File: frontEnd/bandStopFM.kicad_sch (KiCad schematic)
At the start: 18 parts, among them U301 BGS12P2L6E6327XTSA1, U302 BGS12P2L6E6327XTSA1

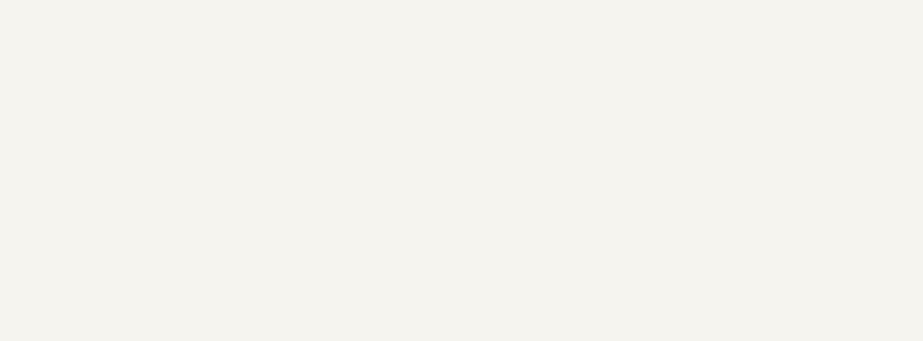
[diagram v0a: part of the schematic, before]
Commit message: update schematics, add bypass for the attenuator
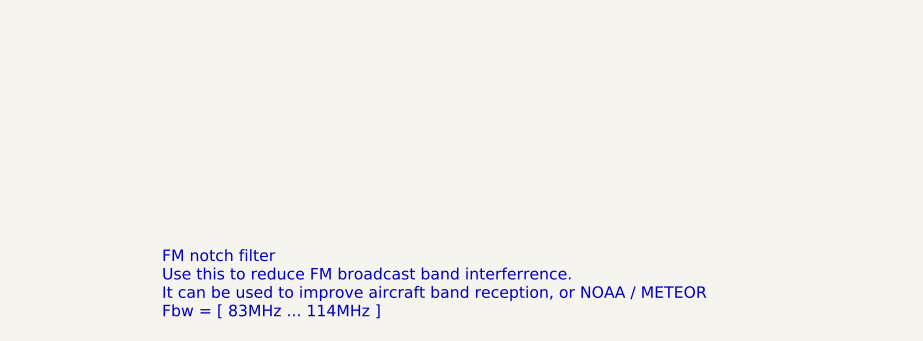
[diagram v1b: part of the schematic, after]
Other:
- note added: "FM notch filter Use this to reduce FM broadcast band interferrence. It can be used to improve aircraft band reception, or NOAA / METEOR Fbw = [ 83MHz ... 114MHz ]"
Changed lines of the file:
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@@
     (stroke (width 0) (type default) (color 0 0 0 0))
+  )
+  (text "FM notch filter\nUse this to reduce FM broadcast band interferrence.\nIt can be used to improve aircraft band reception, or NOAA / METEOR\nFbw = [ 83MHz ... 114MHz ]"
+    (at 180.34 177.8 0)
+    (effects (font (size 1.27 1.27)) (justify left bottom))
   )
   (hierarchical_label "FILTER_ENABLE" (shape input) (at 57.15 83.82 180)

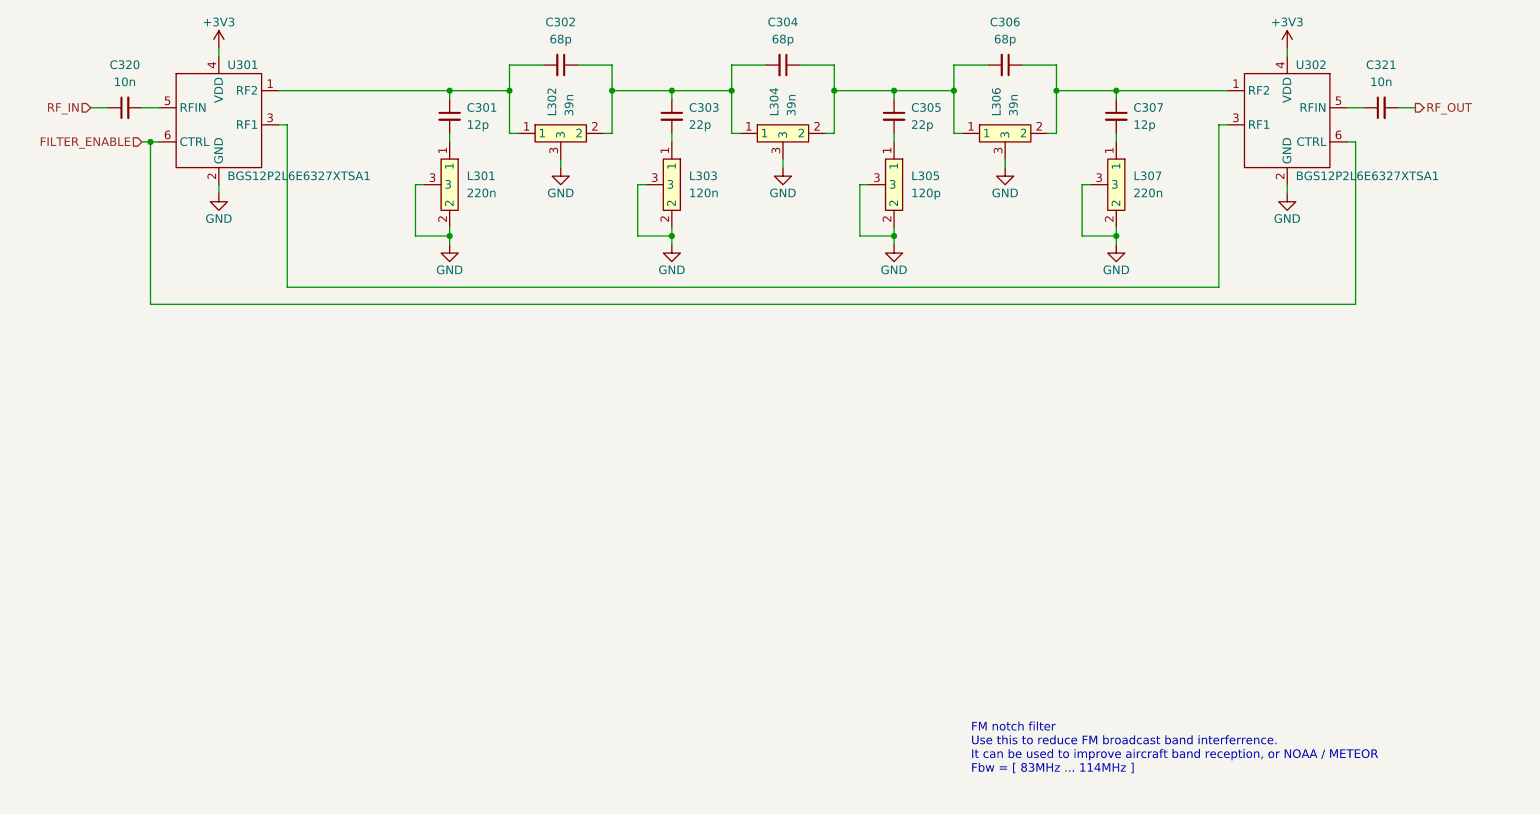
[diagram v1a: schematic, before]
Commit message: simply schematic: remove attenuator and gain blocks; add 5 way multiplexer
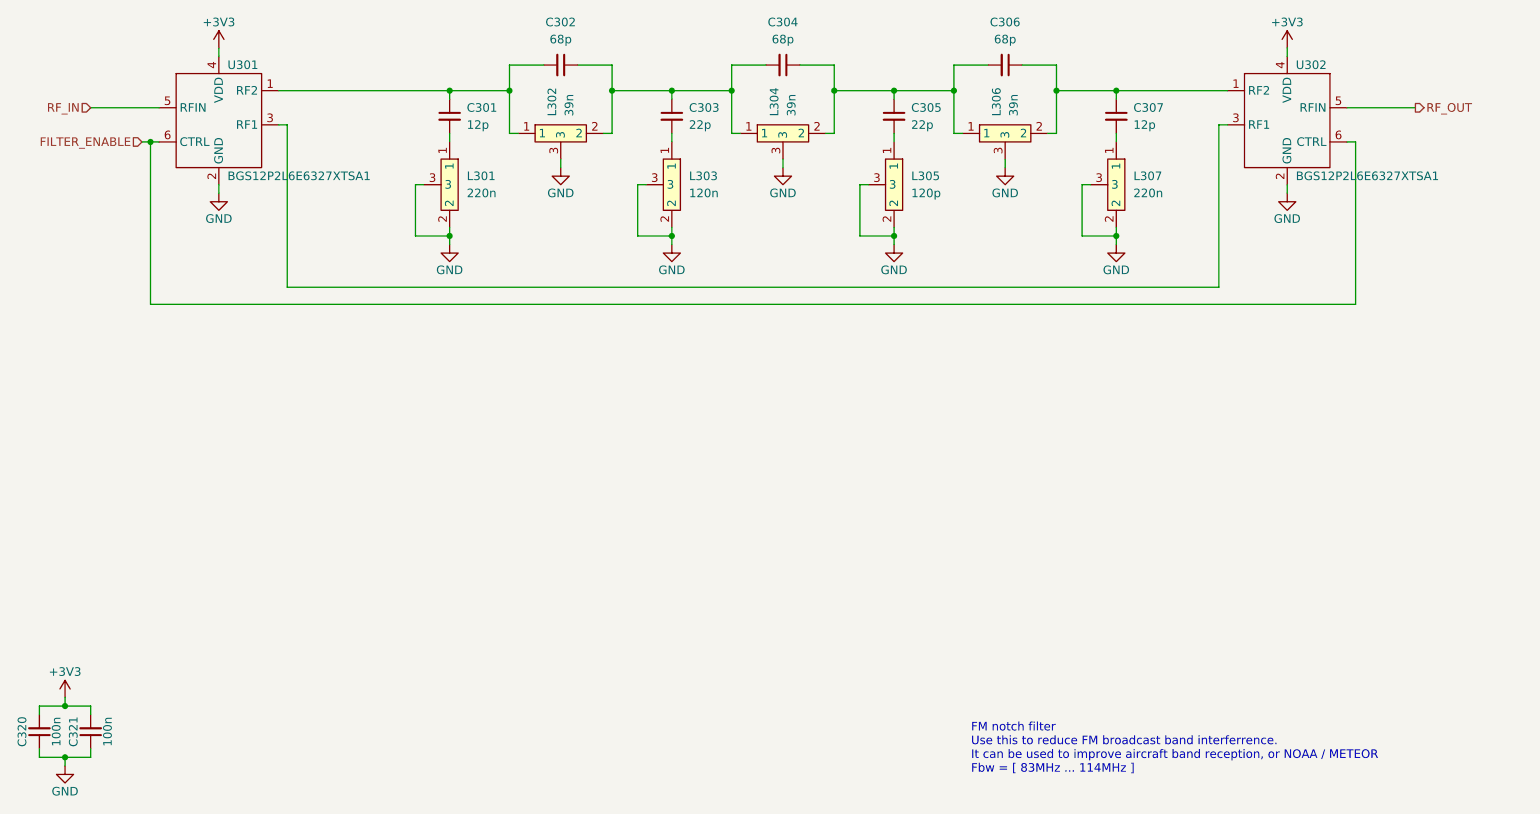
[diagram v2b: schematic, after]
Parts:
- C320, C321: value 10n -> 100n
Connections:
- net +3V3: now also C320.2, C321.2
- net GND: now also C320.1, C321.1
- net RF_IN: now also U301.5 (RFIN); no longer C320.1
- net RF_OUT: now also U302.5 (RFIN); no longer C321.2
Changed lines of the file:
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@@
   (junction (at 193.04 76.2) (diameter 0) (color 0 0 0 0)
   )
+  (junction (at 45.72 167.64) (diameter 0) (color 0 0 0 0)
+  )
   (junction (at 102.87 76.2) (diameter 0) (color 0 0 0 0)
   )
+  (junction (at 45.72 175.26) (diameter 0) (color 0 0 0 0)
+  )
   (junction (at 201.93 97.79) (diameter 0) (color 0 0 0 0)
   )
@@
   (junction (at 201.93 76.2) (diameter 0) (color 0 0 0 0)
   )
+  (wire (pts (xy 41.91 173.99) (xy 41.91 175.26))
+    (stroke (width 0) (type default) (color 0 0 0 0))
+  )
   (wire (pts (xy 152.4 86.36) (xy 152.4 87.63))
     (stroke (width 0) (type default) (color 0 0 0 0))
@@
     (stroke (width 0) (type default) (color 0 0 0 0))
   )
+  (wire (pts (xy 41.91 175.26) (xy 45.72 175.26))
+    (stroke (width 0) (type default) (color 0 0 0 0))
+  )
   (wire (pts (xy 168.91 82.55) (xy 168.91 83.82))
     (stroke (width 0) (type default) (color 0 0 0 0))
@@
     (stroke (width 0) (type default) (color 0 0 0 0))
   )
+  (wire (pts (xy 41.91 168.91) (xy 41.91 167.64))
+    (stroke (width 0) (type default) (color 0 0 0 0))
+  )
   (wire (pts (xy 102.87 97.79) (xy 102.87 99.06))
     (stroke (width 0) (type default) (color 0 0 0 0))
@@
     (stroke (width 0) (type default) (color 0 0 0 0))
   )
-  (wire (pts (xy 57.15 78.74) (xy 59.69 78.74))
+  (wire (pts (xy 45.72 175.26) (xy 45.72 176.53))
     (stroke (width 0) (type default) (color 0 0 0 0))
   )
@@
     (stroke (width 0) (type default) (color 0 0 0 0))
   )
-  (wire (pts (xy 243.84 78.74) (xy 246.38 78.74))
-    (stroke (width 0) (type default) (color 0 0 0 0))
-  )
   (wire (pts (xy 201.93 97.79) (xy 201.93 99.06))
     (stroke (width 0) (type default) (color 0 0 0 0))
@@
     (stroke (width 0) (type default) (color 0 0 0 0))
   )
+  (wire (pts (xy 41.91 167.64) (xy 45.72 167.64))
+    (stroke (width 0) (type default) (color 0 0 0 0))
+  )
   (wire (pts (xy 57.15 83.82) (xy 58.42 83.82))
     (stroke (width 0) (type default) (color 0 0 0 0))
   )
+  (wire (pts (xy 45.72 167.64) (xy 49.53 167.64))
+    (stroke (width 0) (type default) (color 0 0 0 0))
+  )
   (wire (pts (xy 163.83 97.79) (xy 168.91 97.79))
     (stroke (width 0) (type default) (color 0 0 0 0))
@@
     (stroke (width 0) (type default) (color 0 0 0 0))
   )
+  (wire (pts (xy 49.53 167.64) (xy 49.53 168.91))
+    (stroke (width 0) (type default) (color 0 0 0 0))
+  )
   (wire (pts (xy 168.91 76.2) (xy 177.8 76.2))
     (stroke (width 0) (type default) (color 0 0 0 0))
@@
     (stroke (width 0) (type default) (color 0 0 0 0))
   )
+  (wire (pts (xy 49.53 173.99) (xy 49.53 175.26))
+    (stroke (width 0) (type default) (color 0 0 0 0))
+  )
   (wire (pts (xy 165.1 90.17) (xy 163.83 90.17))
     (stroke (width 0) (type default) (color 0 0 0 0))
@@
     (stroke (width 0) (type default) (color 0 0 0 0))
   )
+  (wire (pts (xy 45.72 175.26) (xy 49.53 175.26))
+    (stroke (width 0) (type default) (color 0 0 0 0))
+  )
   (wire (pts (xy 78.74 81.28) (xy 78.74 105.41))
     (stroke (width 0) (type default) (color 0 0 0 0))
@@
     (stroke (width 0) (type default) (color 0 0 0 0))
   )
-  (wire (pts (xy 236.22 78.74) (xy 238.76 78.74))
+  (wire (pts (xy 236.22 78.74) (xy 246.38 78.74))
     (stroke (width 0) (type default) (color 0 0 0 0))
   )
@@
     (stroke (width 0) (type default) (color 0 0 0 0))
   )
-  (wire (pts (xy 49.53 78.74) (xy 52.07 78.74))
+  (wire (pts (xy 49.53 78.74) (xy 59.69 78.74))
+    (stroke (width 0) (type default) (color 0 0 0 0))
+  )
+  (wire (pts (xy 45.72 166.37) (xy 45.72 167.64))
     (stroke (width 0) (type default) (color 0 0 0 0))
   )
@@
     (pin "2")
   )
+  (symbol (lib_id "Device:C_Small") (at 41.91 171.45 180) (unit 1)
+    (in_bom yes) (on_board yes)
+    (property "Reference" "C320" (id 0) (at 39.37 171.45 90))
+    (property "Value" "100n" (id 1) (at 44.45 171.45 90))
+    (property "Footprint" "Capacitor_SMD:C_0805_2012Metric" (id 2) (at 41.91 171.45 0)
+      (effects (font (size 1.27 1.27)) hide)
+    )
+    (property "Datasheet" "~" (id 3) (at 41.91 171.45 0)
+      (effects (font (size 1.27 1.27)) hide)
+    )
+    (pin "1")
+    (pin "2")
+  )
   (symbol (lib_id "frontEnd:DIY_COIL") (at 102.87 90.17 270) (unit 1)
     (in_bom yes) (on_board yes)
@@
     (pin "3")
   )
-  (symbol (lib_id "Device:C_Small") (at 54.61 78.74 90) (unit 1)
-    (in_bom yes) (on_board yes) (fields_autoplaced)
-    (property "Reference" "C320" (id 0) (at 54.6163 72.39 90))
-    (property "Value" "10n" (id 1) (at 54.6163 74.93 90))
-    (property "Footprint" "Capacitor_SMD:C_0805_2012Metric" (id 2) (at 54.61 78.74 0)
-      (effects (font (size 1.27 1.27)) hide)
-    )
-    (property "Datasheet" "~" (id 3) (at 54.61 78.74 0)
-      (effects (font (size 1.27 1.27)) hide)
-    )
-    (pin "1")
-    (pin "2")
+  (symbol (lib_id "power:GND") (at 45.72 176.53 0) (unit 1)
+    (in_bom yes) (on_board yes)
+    (property "Reference" "#PWR?" (id 0) (at 45.72 182.88 0)
+      (effects (font (size 1.27 1.27)) hide)
+    )
+    (property "Value" "GND" (id 1) (at 45.72 180.34 0))
+    (property "Footprint" "" (id 2) (at 45.72 176.53 0)
+      (effects (font (size 1.27 1.27)) hide)
+    )
+    (property "Datasheet" "" (id 3) (at 45.72 176.53 0)
+      (effects (font (size 1.27 1.27)) hide)
+    )
+    (pin "1")
   )
   (symbol (lib_id "Device:C_Small") (at 135.89 80.01 0) (unit 1)
@@
     (pin "2")
   )
+  (symbol (lib_id "power:+3V3") (at 45.72 166.37 0) (unit 1)
+    (in_bom yes) (on_board yes)
+    (property "Reference" "#PWR?" (id 0) (at 45.72 170.18 0)
+      (effects (font (size 1.27 1.27)) hide)
+    )
+    (property "Value" "+3V3" (id 1) (at 45.72 162.56 0))
+    (property "Footprint" "" (id 2) (at 45.72 166.37 0)
+      (effects (font (size 1.27 1.27)) hide)
+    )
+    (property "Datasheet" "" (id 3) (at 45.72 166.37 0)
+      (effects (font (size 1.27 1.27)) hide)
+    )
+    (pin "1")
+  )
   (symbol (lib_id "Device:C_Small") (at 201.93 80.01 0) (unit 1)
     (in_bom yes) (on_board yes) (fields_autoplaced)
@@
     (pin "1")
   )
+  (symbol (lib_id "Device:C_Small") (at 49.53 171.45 180) (unit 1)
+    (in_bom yes) (on_board yes)
+    (property "Reference" "C321" (id 0) (at 46.99 171.45 90))
+    (property "Value" "100n" (id 1) (at 52.07 171.45 90))
+    (property "Footprint" "Capacitor_SMD:C_0805_2012Metric" (id 2) (at 49.53 171.45 0)
+      (effects (font (size 1.27 1.27)) hide)
+    )
+    (property "Datasheet" "~" (id 3) (at 49.53 171.45 0)
+      (effects (font (size 1.27 1.27)) hide)
+    )
+    (pin "1")
+    (pin "2")
+  )
   (symbol (lib_id "frontEnd:DIY_COIL") (at 119.38 82.55 0) (unit 1)
     (in_bom yes) (on_board yes)
@@
     (pin "3")
   )
-  (symbol (lib_id "Device:C_Small") (at 241.3 78.74 90) (unit 1)
-    (in_bom yes) (on_board yes) (fields_autoplaced)
-    (property "Reference" "C321" (id 0) (at 241.3063 72.39 90))
-    (property "Value" "10n" (id 1) (at 241.3063 74.93 90))
-    (property "Footprint" "Capacitor_SMD:C_0805_2012Metric" (id 2) (at 241.3 78.74 0)
-      (effects (font (size 1.27 1.27)) hide)
-    )
-    (property "Datasheet" "~" (id 3) (at 241.3 78.74 0)
-      (effects (font (size 1.27 1.27)) hide)
-    )
-    (pin "1")
-    (pin "2")
-  )
   (symbol (lib_id "frontEnd:BGS12P2L6E6327XTSA1") (at 62.23 78.74 0) (unit 1)
